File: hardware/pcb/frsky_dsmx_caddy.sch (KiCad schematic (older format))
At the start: 24 parts, among them P1 CONN_6, P2 CONN_5, P3 CONN_6X2, Q1 BC847C, Q2 Si2319DS, Q3 Si2319DS, U1 78L05, U2 LN-6206-30

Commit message: Fixed G9X v4.2 (trunk) 3D-setting for the six push button switches. *shrug*
Started TX MOudle Caddy PCB layout.
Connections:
- wire segments 76 -> 58
- no-connect marks 0 -> 9
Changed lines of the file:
@@
-EESchema Schematic File Version 2  date 10/09/2012 10:45:55 a.m.
+EESchema Schematic File Version 2  date 10/09/2012 11:50:27 a.m.
 LIBS:gruvin
 LIBS:power
@@
 LIBS:contrib
 LIBS:valves
+LIBS:frsky_dsmx_caddy-cache
 EELAYER 25  0
 EELAYER END
@@
 $EndDescr
 Wire Wire Line
-	3800 4150 3800 4450
+	3600 4750 9500 4750
+Wire Wire Line
+	9500 4750 9500 2650
+Wire Wire Line
+	9500 2650 10150 2650
+Connection ~ 3800 3300
+Wire Wire Line
+	3800 3750 3800 2950
+Wire Wire Line
+	3800 2950 3950 2950
+Wire Wire Line
+	1250 3300 3800 3300
+Wire Wire Line
+	5450 2150 5450 2350
+Connection ~ 5450 2250
+Wire Wire Line
+	6150 4000 6150 3900
+Wire Wire Line
+	9000 4000 9000 3900
+Wire Wire Line
+	4650 4000 4650 4100
+Wire Wire Line
+	1750 3400 1750 4750
+Wire Wire Line
+	1750 4750 2300 4750
+Connection ~ 8600 3900
+Connection ~ 8600 3500
+Connection ~ 9000 3500
+Wire Wire Line
+	9000 3900 6150 3900
+Connection ~ 1750 3400
+Wire Wire Line
+	2550 3050 2550 3400
+Wire Wire Line
+	10150 2150 9100 2150
+Wire Wire Line
+	9100 2150 9100 2350
+Wire Wire Line
+	4450 2950 4450 2950
+Wire Wire Line
+	4750 2750 4750 2650
+Wire Wire Line
+	6100 1450 2100 1450
+Wire Wire Line
+	2100 1450 2100 3100
+Wire Wire Line
+	2100 3100 1250 3100
+Wire Wire Line
+	6100 1850 5800 1850
+Wire Wire Line
+	1250 3500 2800 3500
+Connection ~ 5750 3850
+Wire Wire Line
+	5650 3850 5750 3850
+Connection ~ 4650 3500
+Wire Wire Line
+	7600 3500 7150 3500
+Wire Wire Line
+	4650 3500 4650 3600
+Wire Wire Line
+	8400 3500 9350 3500
+Wire Wire Line
+	4550 1750 3600 1750
+Wire Wire Line
+	4750 2050 4750 2150
+Connection ~ 6750 3900
+Wire Wire Line
+	4750 3150 4750 3250
+Connection ~ 6150 3500
+Connection ~ 7400 3900
+Wire Wire Line
+	6100 1750 4950 1750
+Wire Wire Line
+	8000 3900 8000 3800
+Connection ~ 7400 3500
+Wire Wire Line
+	5750 3900 5750 3800
+Wire Wire Line
+	5750 4450 3800 4450
+Wire Wire Line
+	5750 4450 5750 4400
+Wire Wire Line
+	3600 1750 3600 3500
+Connection ~ 3600 3500
+Wire Wire Line
+	4600 2100 4750 2100
+Connection ~ 4750 2100
+Wire Wire Line
+	3300 3500 5550 3500
+Wire Wire Line
+	6100 1650 2550 1650
+Wire Wire Line
+	2550 3400 1250 3400
+Wire Wire Line
+	6100 1550 2200 1550
+Wire Wire Line
+	2200 1550 2200 3200
+Wire Wire Line
+	2200 3200 1250 3200
+Wire Wire Line
+	9350 3500 9350 2250
+Wire Wire Line
+	9350 2250 10150 2250
+Connection ~ 8000 3900
+Wire Wire Line
+	2550 1650 2550 2650
+Wire Wire Line
+	6350 3500 5950 3500
+Wire Wire Line
+	3100 4750 2700 4750
+Wire Wire Line
+	1250 3600 1400 3600
+Wire Wire Line
+	1400 3600 1400 3850
+Wire Wire Line
+	5450 2250 5800 2250
+Connection ~ 5450 1750
+Wire Wire Line
+	6750 3900 6750 3800
+Wire Wire Line
+	5800 2250 5800 1850
+Wire Wire Line
+	5150 3850 5050 3850
+Wire Wire Line
+	5050 3850 5050 3500
+Connection ~ 5050 3500
+Wire Wire Line
+	4100 2100 4000 2100
+Wire Wire Line
+	4000 2100 4000 1750
 Connection ~ 4000 1750
 Wire Wire Line
-	4000 1750 4000 2100
-Wire Wire Line
-	4000 2100 4100 2100
-Connection ~ 5050 3500
-Wire Wire Line
-	5050 3500 5050 3850
-Wire Wire Line
-	5050 3850 5150 3850
-Wire Wire Line
-	5800 2250 5800 1850
-Wire Wire Line
-	6750 3800 6750 3900
-Connection ~ 5450 1750
-Wire Wire Line
-	5800 2250 5450 2250
-Wire Wire Line
-	1400 3850 1400 3600
-Wire Wire Line
-	1400 3600 1250 3600
-Wire Wire Line
-	3100 4750 2700 4750
-Wire Wire Line
-	6350 3500 6150 3500
-Wire Wire Line
-	6150 3500 5950 3500
-Wire Wire Line
-	2550 2650 2550 1650
-Wire Wire Line
-	10150 2650 9550 2650
-Connection ~ 8000 3900
-Wire Wire Line
-	10150 2250 9350 2250
-Wire Wire Line
-	9350 2250 9350 3500
-Wire Wire Line
-	1250 3200 2200 3200
-Wire Wire Line
-	2200 3200 2200 1550
-Wire Wire Line
-	2200 1550 6100 1550
-Wire Wire Line
-	1250 3400 1750 3400
-Wire Wire Line
-	1750 3400 2550 3400
-Wire Wire Line
-	2550 1650 6100 1650
-Wire Wire Line
-	3300 3500 3600 3500
-Wire Wire Line
-	3600 3500 4650 3500
-Wire Wire Line
-	4650 3500 5050 3500
-Wire Wire Line
-	5050 3500 5550 3500
-Connection ~ 4750 2100
-Wire Wire Line
-	4600 2100 4750 2100
-Connection ~ 3600 3500
-Wire Wire Line
-	3600 3500 3600 1750
-Wire Wire Line
-	5750 4400 5750 4450
-Wire Wire Line
-	5750 4450 3800 4450
-Wire Wire Line
-	5750 3900 5750 3850
-Wire Wire Line
-	5750 3850 5750 3800
-Connection ~ 7400 3500
-Wire Wire Line
-	8000 3900 8000 3800
-Wire Wire Line
-	6100 1750 5450 1750
-Wire Wire Line
-	5450 1750 4950 1750
-Connection ~ 7400 3900
-Connection ~ 6150 3500
-Wire Wire Line
-	4750 3150 4750 3250
-Connection ~ 6750 3900
-Wire Wire Line
-	4750 2050 4750 2100
-Wire Wire Line
-	4750 2100 4750 2150
-Wire Wire Line
-	3600 1750 4000 1750
-Wire Wire Line
-	4000 1750 4550 1750
-Wire Wire Line
-	9350 3500 9000 3500
-Wire Wire Line
-	9000 3500 8600 3500
-Wire Wire Line
-	8600 3500 8400 3500
-Wire Wire Line
-	4650 3500 4650 3600
-Wire Wire Line
-	7600 3500 7400 3500
-Wire Wire Line
-	7400 3500 7150 3500
-Connection ~ 4650 3500
-Wire Wire Line
-	5650 3850 5750 3850
-Connection ~ 5750 3850
-Wire Wire Line
-	1250 3500 2800 3500
-Wire Wire Line
-	5800 1850 6100 1850
-Wire Wire Line
-	1250 3100 2100 3100
-Wire Wire Line
-	2100 3100 2100 1450
-Wire Wire Line
-	2100 1450 6100 1450
-Wire Wire Line
-	4750 2750 4750 2650
-Wire Wire Line
-	4450 2950 4450 2950
-Wire Wire Line
-	9100 2350 9100 2150
-Wire Wire Line
-	9100 2150 10150 2150
-Wire Wire Line
-	2550 3400 2550 3050
-Connection ~ 1750 3400
-Wire Wire Line
-	9000 3900 8600 3900
-Wire Wire Line
-	8600 3900 8000 3900
-Wire Wire Line
-	8000 3900 7400 3900
-Wire Wire Line
-	7400 3900 6750 3900
-Wire Wire Line
-	6750 3900 6150 3900
-Connection ~ 9000 3500
-Connection ~ 8600 3500
-Connection ~ 8600 3900
-Wire Wire Line
-	9550 2650 9550 4750
-Wire Wire Line
-	9550 4750 3600 4750
-Wire Wire Line
-	2300 4750 1750 4750
-Wire Wire Line
-	1750 4750 1750 3400
-Wire Wire Line
-	4650 4000 4650 4100
-Wire Wire Line
-	9000 3900 9000 4000
-Wire Wire Line
-	6150 3900 6150 4000
-Connection ~ 5450 2250
-Wire Wire Line
-	5450 2150 5450 2250
-Wire Wire Line
-	5450 2250 5450 2350
-Wire Wire Line
-	1250 3300 3800 3300
-Wire Wire Line
-	3950 2950 3800 2950
-Wire Wire Line
-	3800 2950 3800 3300
-Wire Wire Line
-	3800 3300 3800 3750
-Connection ~ 3800 3300
-$Comp
-L GND #PWR6
+	3800 4450 3800 4150
+NoConn ~ 10950 2250
+NoConn ~ 10950 2150
+NoConn ~ 10950 2350
+NoConn ~ 10950 2450
+NoConn ~ 10950 2550
+NoConn ~ 10950 2650
+NoConn ~ 10150 2350
+NoConn ~ 10150 2450
+NoConn ~ 10150 2550
+$Comp
+L GND #PWR01
 U 1 1 504D1983
 P 9000 4000
-F 0 "#PWR6" H 9000 4000 30  0001 C CNN
+F 0 "#PWR01" H 9000 4000 30  0001 C CNN
 F 1 "GND" H 9000 3930 30  0001 C CNN
 	1    9000 4000
@@
 $EndComp
 $Comp
-L GND #PWR2
+L GND #PWR02
 U 1 1 504D1897
 P 4650 4100
-F 0 "#PWR2" H 4650 4100 30  0001 C CNN
+F 0 "#PWR02" H 4650 4100 30  0001 C CNN
 F 1 "GND" H 4650 4030 30  0001 C CNN
 	1    4650 4100
@@
 $EndComp
 $Comp
-L GND #PWR7
+L GND #PWR03
 U 1 1 504D13B3
 P 9100 2350
-F 0 "#PWR7" H 9100 2350 30  0001 C CNN
+F 0 "#PWR03" H 9100 2350 30  0001 C CNN
 F 1 "GND" H 9100 2280 30  0001 C CNN
 	1    9100 2350
@@
 PPM
 $Comp
-L GND #PWR4
+L GND #PWR04
 U 1 1 504D1165
 P 5450 2350
-F 0 "#PWR4" H 5450 2350 30  0001 C CNN
+F 0 "#PWR04" H 5450 2350 30  0001 C CNN
 F 1 "GND" H 5450 2280 30  0001 C CNN
 	1    5450 2350
@@
 BATT+
 $Comp
-L GND #PWR1
+L GND #PWR05
 U 1 1 504D1086
 P 1400 3850
-F 0 "#PWR1" H 1400 3850 30  0001 C CNN
+F 0 "#PWR05" H 1400 3850 30  0001 C CNN
 F 1 "GND" H 1400 3780 30  0001 C CNN
 	1    1400 3850
@@
 $EndComp
 $Comp
-L GND #PWR3
+L GND #PWR06
 U 1 1 4E7B4B20
 P 4750 3250
-F 0 "#PWR3" H 4750 3250 30  0001 C CNN
+F 0 "#PWR06" H 4750 3250 30  0001 C CNN
 F 1 "GND" H 4750 3180 30  0001 C CNN
 	1    4750 3250
@@
 $EndComp
 $Comp
-L GND #PWR5
+L GND #PWR07
 U 1 1 4E1493B8
 P 6150 4000
-F 0 "#PWR5" H 6150 4000 30  0001 C CNN
+F 0 "#PWR07" H 6150 4000 30  0001 C CNN
 F 1 "GND" H 6150 3930 30  0001 C CNN
 	1    6150 4000

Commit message: TX Moudle Caddy PCB completed.
Some missing files added.
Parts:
- F1: value FUSE -> 250mA
- P1: value CONN_6 -> G9X
- P2: value CONN_5 -> Fr-Sky
- P3: value CONN_6X2 -> DSMX
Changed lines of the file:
@@
-EESchema Schematic File Version 2  date 10/09/2012 11:50:27 a.m.
+EESchema Schematic File Version 2  date 10/09/2012 4:18:02 p.m.
 LIBS:gruvin
 LIBS:power
@@
 Sheet 1 1
 Title "Fr-Sky / DSMX TX Moudle Caddy"
-Date "9 sep 2012"
+Date "10 sep 2012"
 Rev "1.0"
 Comp ""
@@
 P 6500 1650
 F 0 "P2" V 6450 1650 50  0000 C CNN
-F 1 "CONN_5" V 6550 1650 50  0000 C CNN
+F 1 "Fr-Sky" V 6550 1650 50  0000 C CNN
 	1    6500 1650
 	1    0    0    1
@@
 P 10550 2400
 F 0 "P3" H 10550 2750 60  0000 C CNN
-F 1 "CONN_6X2" V 10550 2400 60  0000 C CNN
+F 1 "DSMX" V 10550 2400 60  0000 C CNN
 	1    10550 2400
 	1    0    0    -1
@@
 P 900 3350
 F 0 "P1" V 850 3350 60  0000 C CNN
-F 1 "CONN_6" V 950 3350 60  0000 C CNN
+F 1 "G9X" V 950 3350 60  0000 C CNN
 	1    900  3350
 	-1   0    0    1
@@
 P 3050 3500
 F 0 "F1" H 3150 3550 40  0000 C CNN
-F 1 "FUSE" H 2950 3450 40  0000 C CNN
+F 1 "250mA" H 2950 3400 40  0000 C CNN
 	1    3050 3500
 	1    0    0    -1

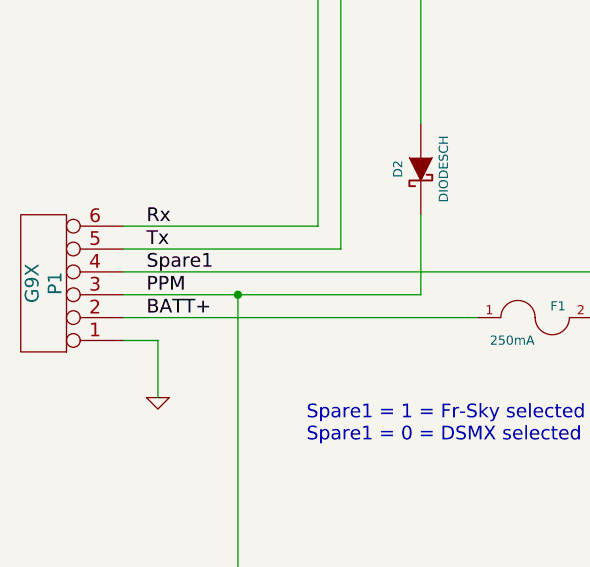
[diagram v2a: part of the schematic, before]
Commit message: Mostly TX caddy work. This version is larger and facilitates mounting the DSMX module such that it lays over top of the caddy board, rather than floating off the end. This will use up less space. I added matching mounting holes too, just in case that comes in handy. *shrug*
There was also an error (missing track) in the v1.0 prototype. I 
decided not to bother building the circuit yet and will instead
wait for the v1.1 boards to arrive. Fingers crossed for luck.

I considered adding a little more circuitry to allow controlling
the Fr-Sky 'togle switch' options, namely F/W Upgrade, One-way and
Two-way modes. Probably shoul dhave done this now, rather than
later ... but I just didn't.

Added a 'CALI' footprint to the module library. I used it as a fiducial 
marker for calibrating my printer. *shrug*

No actual changes to gruvin9x.brd. That was just some plot settings, 
I think.

There's some files added to the repository that probably should have 
been there before, but weren't.
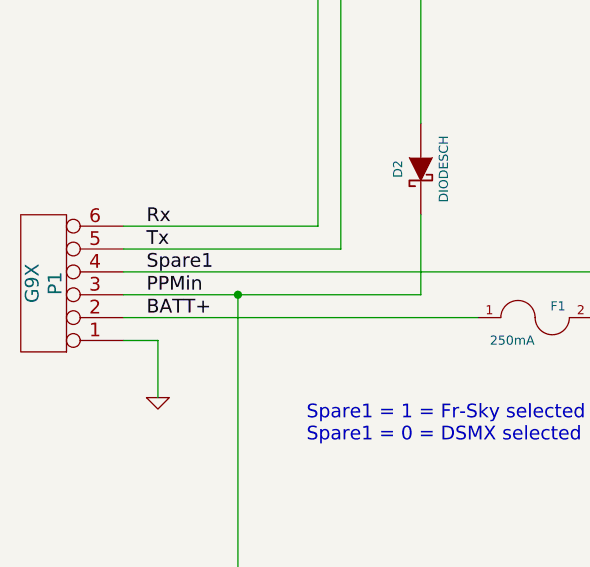
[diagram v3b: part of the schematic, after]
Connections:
- net labels added: PPMin
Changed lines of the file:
@@
-EESchema Schematic File Version 2  date 10/09/2012 4:18:02 p.m.
+EESchema Schematic File Version 2  date Wed 26 Sep 2012 12:52:50 PM NZST
 LIBS:gruvin
 LIBS:power
@@
 Sheet 1 1
 Title "Fr-Sky / DSMX TX Moudle Caddy"
-Date "10 sep 2012"
-Rev "1.0"
+Date "25 sep 2012"
+Rev "1.1"
 Comp ""
 Comment1 ""
@@
 Txd
 Text Label 1350 3400 0    60   ~ 0
-PPM
+PPMin
 $Comp
 L GND #PWR04

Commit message: TX Caddy changes (mostly).
The ITead shopping cart wasn't working when I went to order the previous
version of the TX Caddy board. I took that as an omen and proceeded to add the
feature to allow firmware controlled switching between 1-Way and 2-Way mode on
the Fr-Sky DHT DIY module, after all. (Not sure where to connect that to on 
the main board yet, though.)

Added a PIN_ARRAY_7X1 module for the gruin library.

Apparently, I also changed the new Wings 3D LED parts since they 
were last committed.
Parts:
- added Q4: BC847C, SOT23-BCE, symbol BC847C
- added R7: 5K1, symbol R
- added R8: 100K, symbol R
- added R9: 1K, symbol R
- P1: symbol CONN_6 -> CONN_7
- P2: symbol CONN_5 -> CONN_6
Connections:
- net labels added: 1WAY, 1WSEL
- wire segments 58 -> 70
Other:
- moved on the sheet: D2
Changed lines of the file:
@@
-EESchema Schematic File Version 2  date Wed 26 Sep 2012 12:52:50 PM NZST
+EESchema Schematic File Version 2  date Wed 26 Sep 2012 04:29:42 PM NZST
 LIBS:gruvin
 LIBS:power
@@
 Sheet 1 1
 Title "Fr-Sky / DSMX TX Moudle Caddy"
-Date "25 sep 2012"
-Rev "1.1"
+Date "26 sep 2012"
+Rev "1.2"
 Comp ""
 Comment1 ""
@@
 Comment4 "Licensed under the TAPR Open Hardware License (see file,  LICENSE)"
 $EndDescr
+Text Label 1350 3600 0    60   ~ 0
+1WSEL
+Connection ~ 2550 2750
+Wire Wire Line
+	2550 3050 2550 2750
+Wire Wire Line
+	2550 3050 2700 3050
+Wire Wire Line
+	3100 2750 2350 2750
+Wire Wire Line
+	2350 3250 2350 3600
+Wire Wire Line
+	2350 3600 1250 3600
 Wire Wire Line
 	3600 4750 9500 4750
@@
 Connection ~ 5450 2250
 Wire Wire Line
-	6150 4000 6150 3900
-Wire Wire Line
-	9000 4000 9000 3900
+	6150 3900 6150 4000
+Wire Wire Line
+	9000 3900 9000 4000
 Wire Wire Line
 	4650 4000 4650 4100
 Wire Wire Line
-	1750 3400 1750 4750
+	1750 4750 1750 3400
 Wire Wire Line
 	1750 4750 2300 4750
@@
 Connection ~ 9000 3500
 Wire Wire Line
-	9000 3900 6150 3900
+	6150 3900 9000 3900
 Connection ~ 1750 3400
 Wire Wire Line
-	2550 3050 2550 3400
+	2150 3400 2150 2300
 Wire Wire Line
 	10150 2150 9100 2150
@@
 	4750 2750 4750 2650
 Wire Wire Line
-	6100 1450 2100 1450
-Wire Wire Line
-	2100 1450 2100 3100
-Wire Wire Line
-	2100 3100 1250 3100
-Wire Wire Line
-	6100 1850 5800 1850
+	6250 1450 1750 1450
+Wire Wire Line
+	1750 1450 1750 3100
+Wire Wire Line
+	1750 3100 1250 3100
 Wire Wire Line
 	1250 3500 2800 3500
@@
 Connection ~ 7400 3900
 Wire Wire Line
-	6100 1750 4950 1750
+	6250 1750 4950 1750
 Wire Wire Line
 	8000 3900 8000 3800
@@
 	3300 3500 5550 3500
 Wire Wire Line
-	6100 1650 2550 1650
-Wire Wire Line
-	2550 3400 1250 3400
-Wire Wire Line
-	6100 1550 2200 1550
-Wire Wire Line
-	2200 1550 2200 3200
-Wire Wire Line
-	2200 3200 1250 3200
+	6250 1650 2150 1650
+Wire Wire Line
+	1250 3400 2150 3400
+Wire Wire Line
+	6250 1550 1900 1550
+Wire Wire Line
+	1900 1550 1900 3200
+Wire Wire Line
+	1900 3200 1250 3200
 Wire Wire Line
 	9350 3500 9350 2250
@@
 Connection ~ 8000 3900
 Wire Wire Line
-	2550 1650 2550 2650
+	2150 1650 2150 1900
 Wire Wire Line
 	6350 3500 5950 3500
@@
 	3100 4750 2700 4750
 Wire Wire Line
-	1250 3600 1400 3600
-Wire Wire Line
-	1400 3600 1400 3850
+	1250 3700 1400 3700
+Wire Wire Line
+	1400 3700 1400 3950
 Wire Wire Line
 	5450 2250 5800 2250
 Connection ~ 5450 1750
 Wire Wire Line
-	6750 3900 6750 3800
-Wire Wire Line
-	5800 2250 5800 1850
+	6750 3800 6750 3900
+Wire Wire Line
+	5800 2250 5800 1950
 Wire Wire Line
 	5150 3850 5050 3850
@@
 Wire Wire Line
 	3800 4450 3800 4150
+Wire Wire Line
+	5800 1950 6250 1950
+Wire Wire Line
+	3400 2950 3400 3150
+Wire Wire Line
+	3400 2550 3400 2450
+Wire Wire Line
+	3400 1950 3400 1350
+Wire Wire Line
+	3400 1350 5750 1350
+Wire Wire Line
+	5750 1350 5750 1850
+Wire Wire Line
+	5750 1850 6250 1850
+Wire Wire Line
+	3200 3050 3400 3050
+Connection ~ 3400 3050
+$Comp
+L BC847C Q4
+U 1 1 50627C0F
+P 3300 2750
+F 0 "Q4" H 3150 2650 50  0000 C CNN
+F 1 "BC847C" H 3200 2950 50  0000 C CNN
+F 2 "SOT23-BCE" H 3490 2750 30  0001 C CNN
+	1    3300 2750
+	1    0    0    -1
+$EndComp
+$Comp
+L R R8
+U 1 1 50627D8A
+P 2950 3050
+F 0 "R8" V 2850 3050 50  0000 C CNN
+F 1 "100K" V 2950 3050 50  0000 C CNN
+	1    2950 3050
+	0    1    1    0
+$EndComp
+Text Label 6200 1850 2    60   ~ 0
+1WAY
+$Comp
+L R R9
+U 1 1 50627C10
+P 3400 2200
+F 0 "R9" V 3480 2200 50  0000 C CNN
+F 1 "1K" V 3400 2200 50  0000 C CNN
+	1    3400 2200
+	-1   0    0    1
+$EndComp
+$Comp
+L R R7
+U 1 1 50627C0E
+P 2350 3000
+F 0 "R7" V 2430 3000 50  0000 C CNN
+F 1 "5K1" V 2350 3000 50  0000 C CNN
+	1    2350 3000
+	-1   0    0    1
+$EndComp
+$Comp
+L GND #PWR01
+U 1 1 50627C0D
+P 3400 3150
+F 0 "#PWR01" H 3400 3150 30  0001 C CNN
+F 1 "GND" H 3400 3080 30  0001 C CNN
+	1    3400 3150
+	1    0    0    -1
+$EndComp
 NoConn ~ 10950 2250
 NoConn ~ 10950 2150
@@
 NoConn ~ 10150 2550
 $Comp
-L GND #PWR01
+L GND #PWR02
 U 1 1 504D1983
 P 9000 4000
-F 0 "#PWR01" H 9000 4000 30  0001 C CNN
+F 0 "#PWR02" H 9000 4000 30  0001 C CNN
 F 1 "GND" H 9000 3930 30  0001 C CNN
 	1    9000 4000
@@
 $EndComp
 $Comp
-L GND #PWR02
+L GND #PWR03
 U 1 1 504D1897
 P 4650 4100
-F 0 "#PWR02" H 4650 4100 30  0001 C CNN
+F 0 "#PWR03" H 4650 4100 30  0001 C CNN
 F 1 "GND" H 4650 4030 30  0001 C CNN
 	1    4650 4100
@@
 L DIODESCH D2
 U 1 1 504D14E4
-P 2550 2850
-F 0 "D2" H 2550 2950 40  0000 C CNN
-F 1 "DIODESCH" H 2550 2750 40  0000 C CNN
-	1    2550 2850
+P 2150 2100
+F 0 "D2" H 2150 2200 40  0000 C CNN
+F 1 "DIODESCH" H 2150 2000 40  0000 C CNN
+	1    2150 2100
 	0    -1   1    0
 $EndComp
@@
 $EndComp
 $Comp
-L GND #PWR03
+L GND #PWR04
 U 1 1 504D13B3
 P 9100 2350
-F 0 "#PWR03" H 9100 2350 30  0001 C CNN
+F 0 "#PWR04" H 9100 2350 30  0001 C CNN
 F 1 "GND" H 9100 2280 30  0001 C CNN
 	1    9100 2350
@@
 Text Label 1350 3200 0    60   ~ 0
 Tx
-Text Notes 6250 2050 0    60   ~ 0
+Text Notes 6250 2150 0    60   ~ 0
 Fr-Sky DHT
-Text Label 5850 1850 0    60   ~ 0
+Text Label 6200 1950 2    60   ~ 0
 GND
-Text Label 5850 1750 0    60   ~ 0
+Text Label 6200 1750 2    60   ~ 0
 B+
-Text Label 5850 1650 0    60   ~ 0
+Text Label 6200 1650 2    60   ~ 0
 PPM
-Text Label 5850 1550 0    60   ~ 0
+Text Label 6200 1550 2    60   ~ 0
 Rxd
-Text Label 5850 1450 0    60   ~ 0
+Text Label 6200 1450 2    60   ~ 0
 Txd
 Text Label 1350 3400 0    60   ~ 0
 PPMin
 $Comp
-L GND #PWR04
+L GND #PWR05
 U 1 1 504D1165
 P 5450 2350
-F 0 "#PWR04" H 5450 2350 30  0001 C CNN
+F 0 "#PWR05" H 5450 2350 30  0001 C CNN
 F 1 "GND" H 5450 2280 30  0001 C CNN
 	1    5450 2350
@@
 $EndComp
 $Comp
-L CONN_5 P2
+L CONN_6 P2
 U 1 1 504D1155
-P 6500 1650
-F 0 "P2" V 6450 1650 50  0000 C CNN
-F 1 "Fr-Sky" V 6550 1650 50  0000 C CNN
-	1    6500 1650
+P 6600 1700
+F 0 "P2" V 6550 1700 50  0000 C CNN
+F 1 "Fr-Sky" V 6650 1700 50  0000 C CNN
+	1    6600 1700
 	1    0    0    1
 $EndComp
@@
 BATT+
 $Comp
-L GND #PWR05
+L GND #PWR06
 U 1 1 504D1086
-P 1400 3850
-F 0 "#PWR05" H 1400 3850 30  0001 C CNN
-F 1 "GND" H 1400 3780 30  0001 C CNN
-	1    1400 3850
-	1    0    0    -1
-$EndComp
-$Comp
-L CONN_6 P1
+P 1400 3950
+F 0 "#PWR06" H 1400 3950 30  0001 C CNN
+F 1 "GND" H 1400 3880 30  0001 C CNN
+	1    1400 3950
+	1    0    0    -1
+$EndComp
+$Comp
+L CONN_7 P1
 U 1 1 504D1054
-P 900 3350
-F 0 "P1" V 850 3350 60  0000 C CNN
-F 1 "G9X" V 950 3350 60  0000 C CNN
-	1    900  3350
+P 900 3400
+F 0 "P1" V 850 3400 60  0000 C CNN
+F 1 "G9X" V 950 3400 60  0000 C CNN
+	1    900  3400
 	-1   0    0    1
 $EndComp
@@
 $EndComp
 $Comp
-L GND #PWR06
+L GND #PWR07
 U 1 1 4E7B4B20
 P 4750 3250
-F 0 "#PWR06" H 4750 3250 30  0001 C CNN
+F 0 "#PWR07" H 4750 3250 30  0001 C CNN
 F 1 "GND" H 4750 3180 30  0001 C CNN
 	1    4750 3250
@@
 $EndComp
 $Comp
-L GND #PWR07
+L GND #PWR08
 U 1 1 4E1493B8
 P 6150 4000
-F 0 "#PWR07" H 6150 4000 30  0001 C CNN
+F 0 "#PWR08" H 6150 4000 30  0001 C CNN
 F 1 "GND" H 6150 3930 30  0001 C CNN
 	1    6150 4000
